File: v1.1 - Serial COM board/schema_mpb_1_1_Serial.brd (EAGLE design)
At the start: 93.3 x 48.5 mm, 76 parts, among them U4 MAX232PTH, U5 MAX232PTH, U6 MAX232PTH

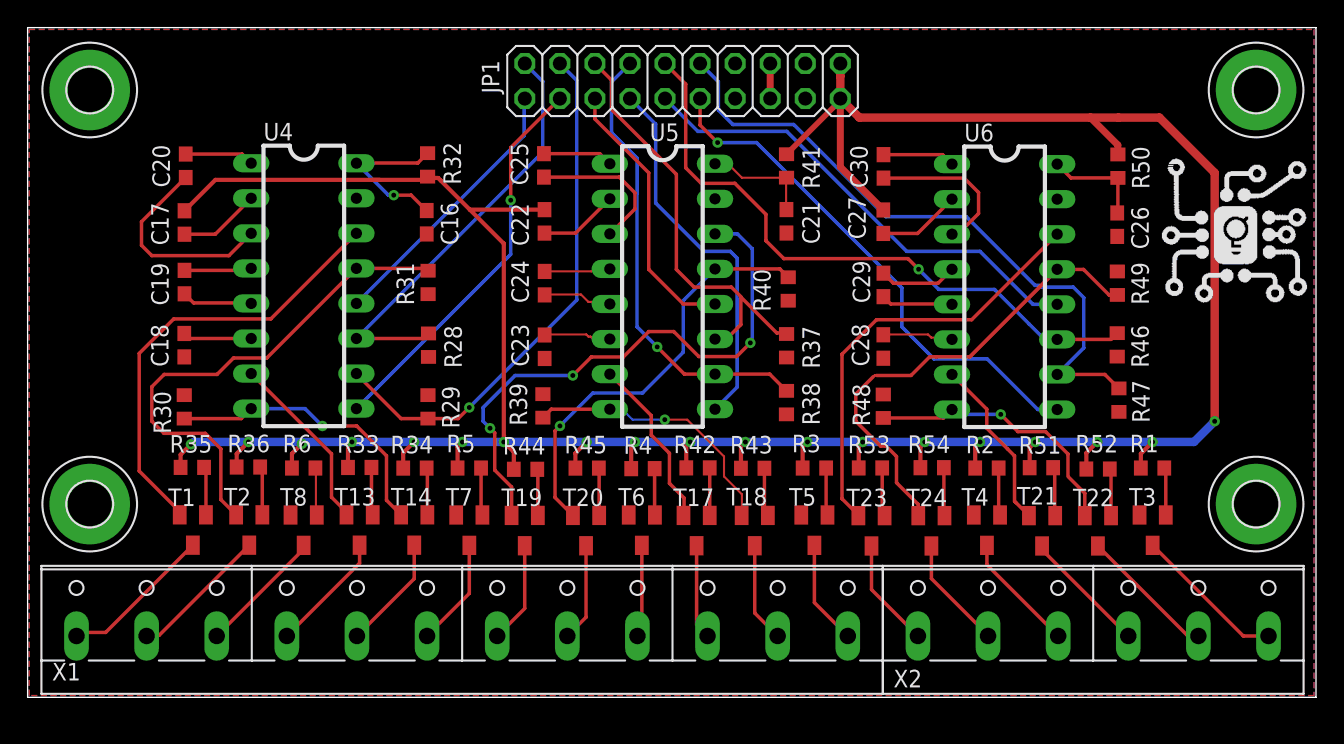
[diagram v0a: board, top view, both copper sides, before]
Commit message: IO and Serial
- Rounded corners
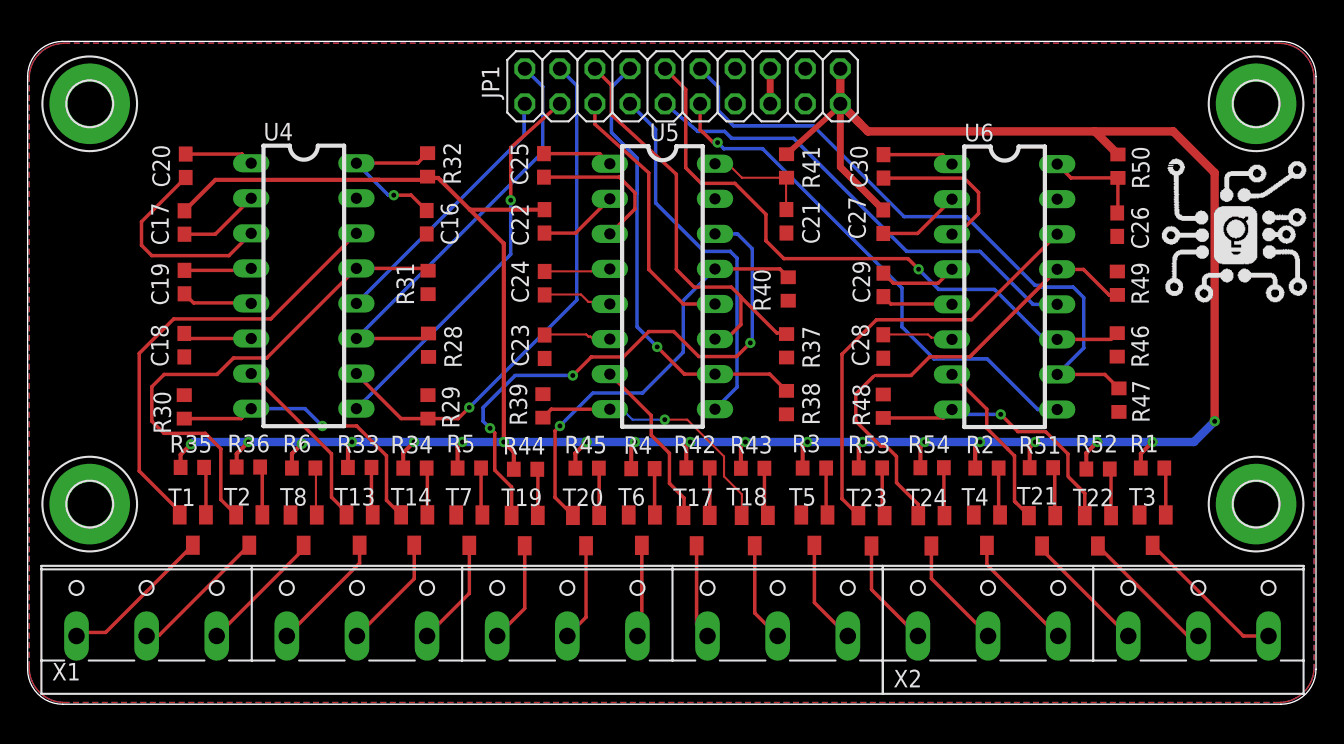
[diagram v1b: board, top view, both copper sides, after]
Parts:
- moved H3 1.00 mm to (3.50, 43.0)
- moved H4 1.00 mm to (88.0, 43.0)
- moved JP1 0.38 mm to (46.5, 44.3)
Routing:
- net +3V3: track 238.2 -> 236.4 mm
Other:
- board size 93.3 x 48.5 mm -> 93.3 x 48 mm

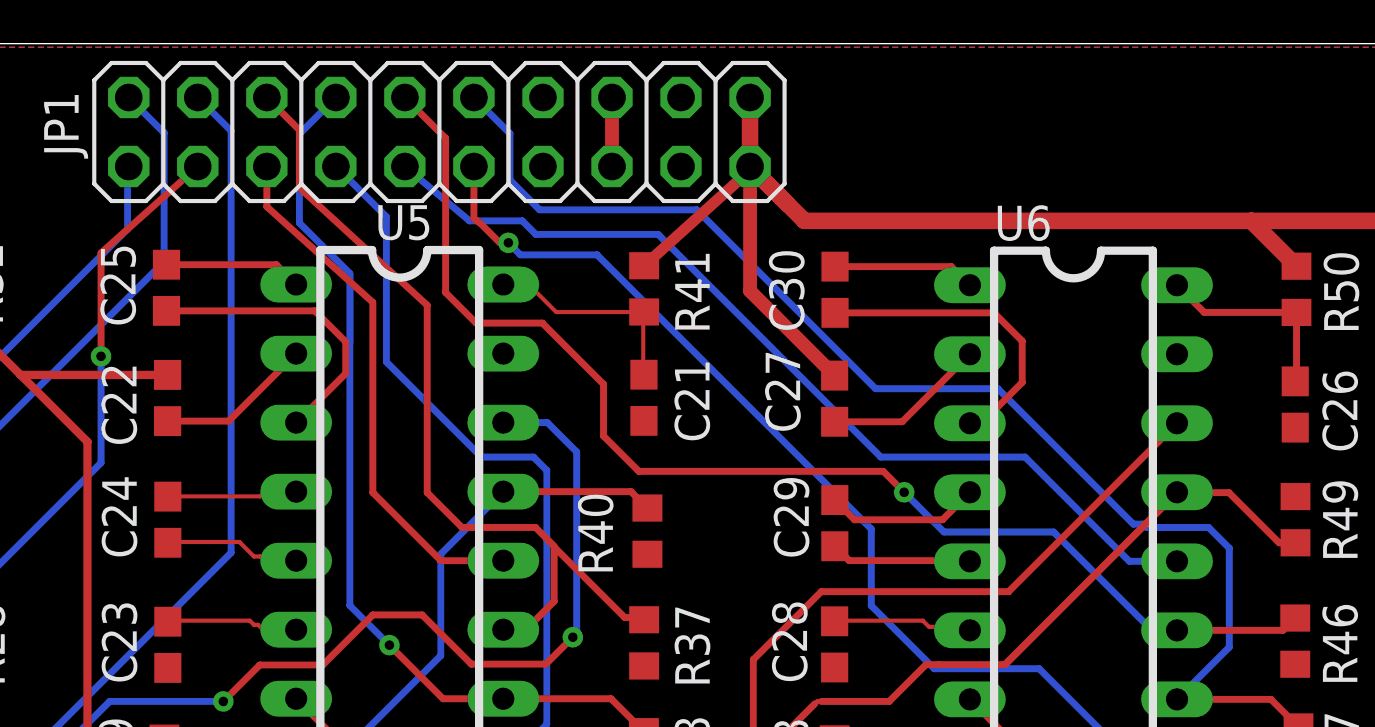
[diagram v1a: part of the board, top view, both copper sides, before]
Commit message: IO board revision
- Made Output traces thicker
- Added pad for 5V/3.3V power for input sensors
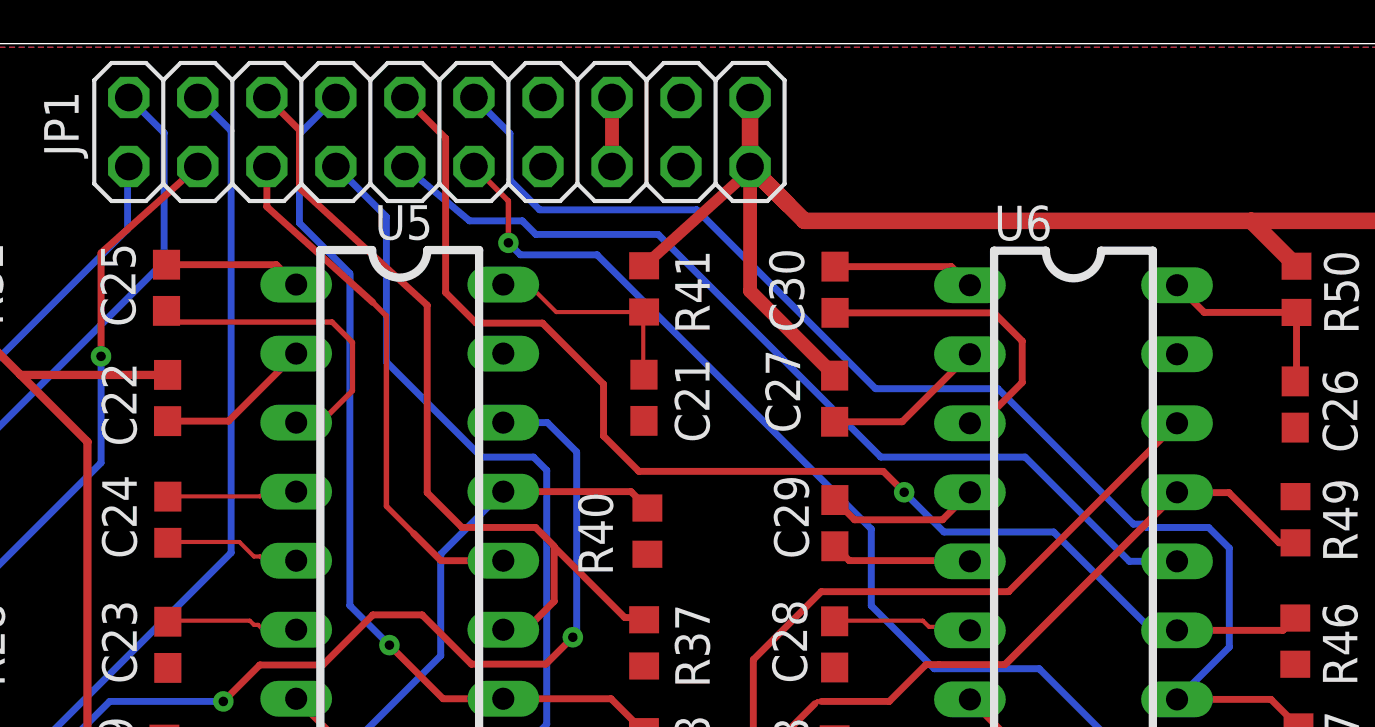
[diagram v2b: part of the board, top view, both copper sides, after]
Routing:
- net N$45: track 11.0 -> 11.8 mm
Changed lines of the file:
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@@
 <wire x1="41.2242" y1="33.6042" x2="41.2242" y2="33.7566" width="0.1524" layer="1"/>
 <wire x1="41.2242" y1="33.6042" x2="41.18" y2="33.576" width="0.1524" layer="1"/>
-<wire x1="36.409" y1="37.687" x2="41.866" y2="37.687" width="0.254" layer="1"/>
-<wire x1="41.866" y1="37.687" x2="43.0022" y2="36.5508" width="0.254" layer="1"/>
-<wire x1="43.0022" y1="35.3822" x2="41.2242" y2="33.6042" width="0.254" layer="1"/>
-<wire x1="43.0022" y1="36.5508" x2="43.0022" y2="35.3822" width="0.254" layer="1"/>
+<wire x1="41.31" y1="33.69" x2="41.2242" y2="33.6042" width="0.254" layer="1"/>
+<wire x1="42.19" y1="33.69" x2="41.31" y2="33.69" width="0.2" layer="1"/>
+<wire x1="43.25" y1="34.75" x2="42.19" y2="33.69" width="0.2" layer="1"/>
+<wire x1="42.5" y1="37.2765" x2="43.25" y2="36.5265" width="0.2" layer="1"/>
+<wire x1="43.25" y1="36.5265" x2="43.25" y2="34.75" width="0.2" layer="1"/>
+<wire x1="36.409" y1="37.687" x2="36.8195" y2="37.2765" width="0.2" layer="1"/>
+<wire x1="36.8195" y1="37.2765" x2="42.5" y2="37.2765" width="0.2" layer="1"/>
 </signal>
 <signal name="N$46">
@@
 <wire x1="40.1" y1="42.999" x2="40.1" y2="41.519" width="0.254" layer="1"/>
 <wire x1="40.1" y1="41.519" x2="44" y2="38" width="0.254" layer="1"/>
-<wire x1="44" y1="38" x2="44" y2="31" width="0.254" layer="1"/>
 <wire x1="46.504" y1="28.496" x2="48.8" y2="28.496" width="0.254" layer="1"/>
-<wire x1="44" y1="31" x2="46.504" y2="28.496" width="0.254" layer="1"/>
+<wire x1="45.5" y1="29.5" x2="46.504" y2="28.496" width="0.254" layer="1"/>
+<wire x1="44" y1="38" x2="44.5" y2="37.5" width="0.2" layer="1"/>
+<wire x1="44.5" y1="30.5" x2="45.5" y2="29.5" width="0.2" layer="1"/>
+<wire x1="44.5" y1="37.5" x2="44.5" y2="30.5" width="0.2" layer="1"/>
 </signal>
 <signal name="RX4">
@@
 <contactref element="U6" pad="9"/>
 <via x="48.9886" y="40.1908" extent="1-16" drill="0.35"/>
-<wire x1="47.72" y1="42.999" x2="47.72" y2="41.0784" width="0.254" layer="1"/>
-<wire x1="47.72" y1="41.0784" x2="47.944803125" y2="40.9211125" width="0.254" layer="1"/>
 <wire x1="62.3397" y1="29.6603" x2="62.3397" y2="26.8397" width="0.254" layer="16"/>
 <wire x1="52.25" y1="39.75" x2="62.3397" y2="29.6603" width="0.254" layer="16"/>
@@
 <wire x1="68.5201" y1="24.5201" x2="72.1882" y2="20.852" width="0.254" layer="16"/>
 <wire x1="72.1882" y1="20.852" x2="73.59" y2="20.852" width="0.254" layer="16"/>
-<wire x1="47.944803125" y1="40.9211125" x2="48.675115625" y2="40.1908" width="0.254" layer="1"/>
-<wire x1="48.675115625" y1="40.1908" x2="48.9886" y2="40.1908" width="0.254" layer="1"/>
 <wire x1="48.9886" y1="40.1908" x2="49.4294" y2="39.75" width="0.254" layer="16"/>
 <wire x1="49.4294" y1="39.75" x2="52.25" y2="39.75" width="0.254" layer="16"/>
+<wire x1="48.9886" y1="40.1908" x2="48.9886" y2="41.7304" width="0.2" layer="1"/>
+<wire x1="48.9886" y1="41.7304" x2="47.72" y2="42.999" width="0.2" layer="1"/>
 </signal>
 <signal name="+5V">
@@
 <wire x1="75.5142" y1="28.956" x2="74.7522" y2="29.718" width="0.254" layer="16"/>
 <wire x1="75.5142" y1="25.3162" x2="75.5142" y2="28.956" width="0.254" layer="16"/>
-<wire x1="74.7522" y1="29.718" x2="72.4662" y2="29.718" width="0.254" layer="16"/>
+<wire x1="74.7522" y1="29.718" x2="74.5" y2="29.718" width="0.254" layer="16"/>
+<wire x1="74.5" y1="29.718" x2="72.4662" y2="29.718" width="0.254" layer="16"/>
 <wire x1="72.4662" y1="29.718" x2="72.3421" y2="29.8421" width="0.254" layer="16"/>
 <wire x1="72.3421" y1="29.8421" x2="71.9813" y2="29.8421" width="0.254" layer="16"/>

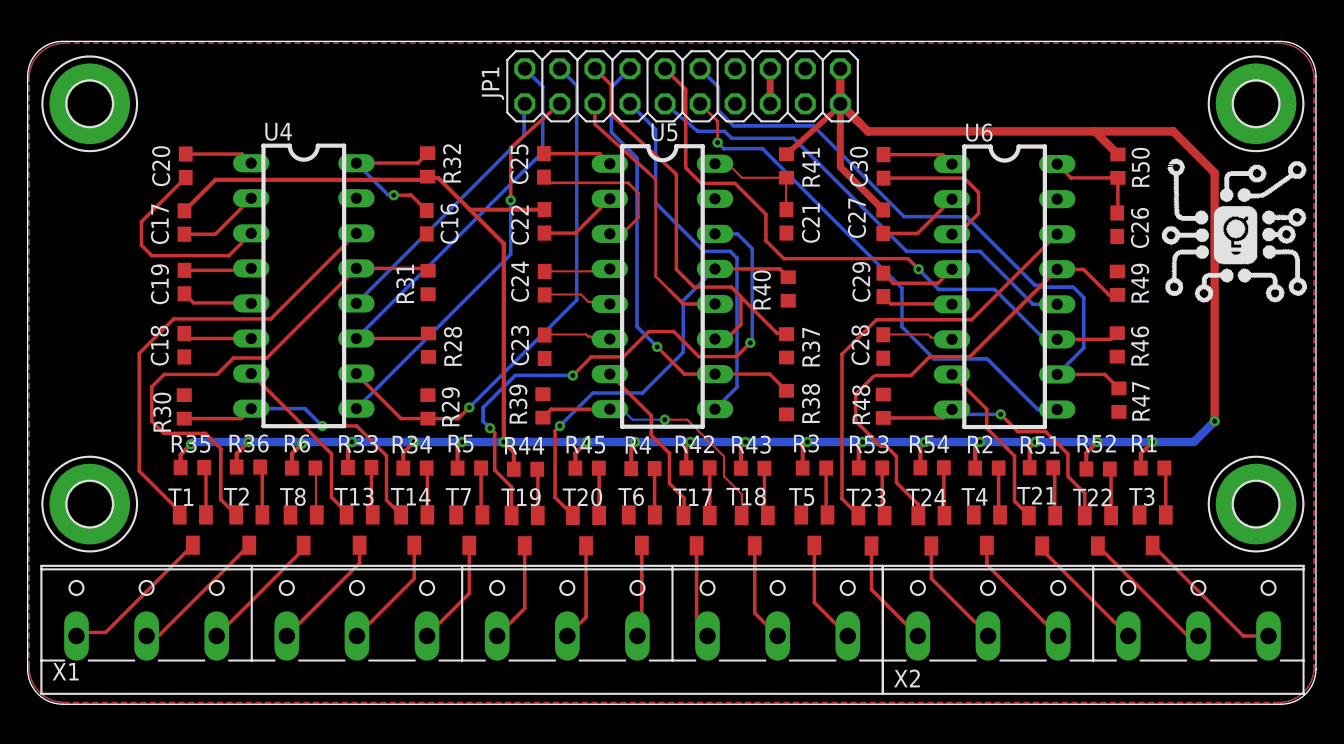
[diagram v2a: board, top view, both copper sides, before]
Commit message: Serial Board Revision
- Labelled terminals
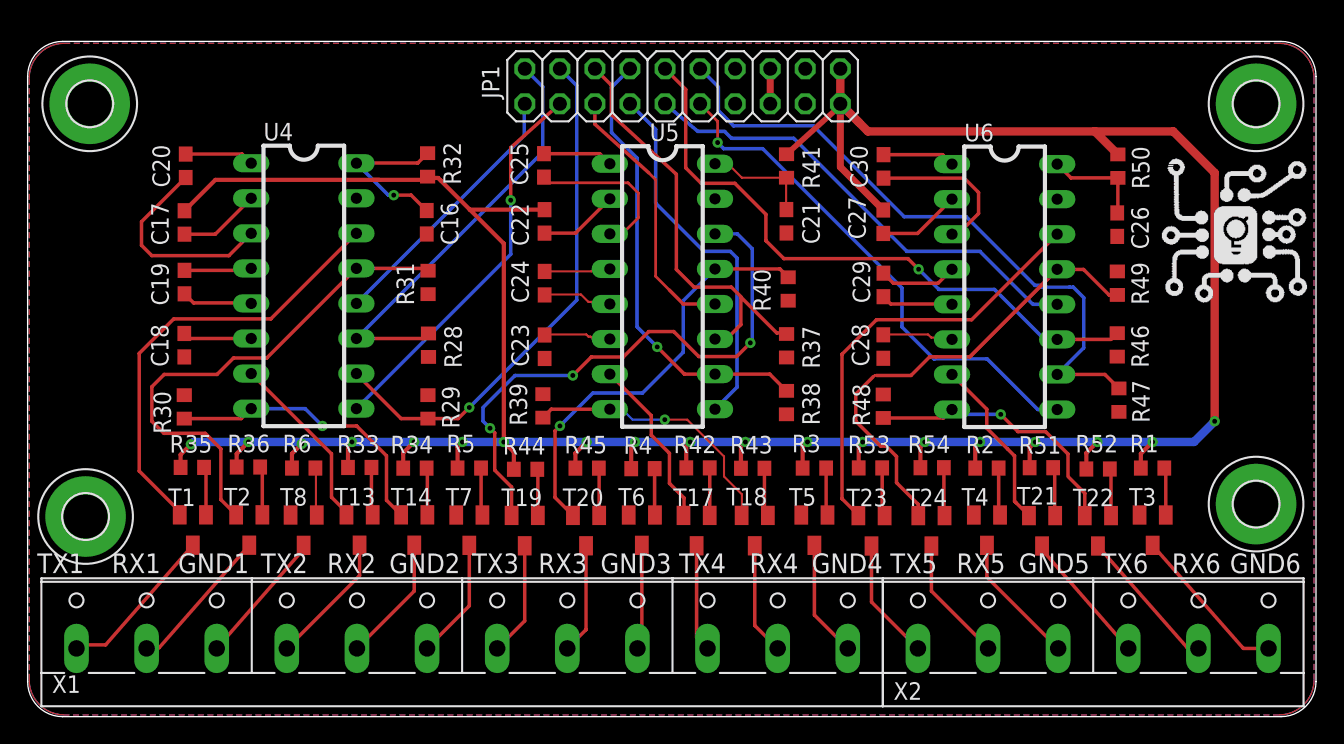
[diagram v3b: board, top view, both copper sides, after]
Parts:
- moved H1 0.95 mm to (3.20, 13.1)
- moved X1 0.90 mm to (30.5, 4.18)
- moved X2 0.90 mm to (76.2, 4.18)
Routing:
- net RXD2#: track 8.29 -> 9.19 mm
- net RXD4#: track 7.22 -> 8.12 mm
- net TXD4#: track 6.86 -> 7.76 mm
- net TXD3#: track 7.36 -> 8.26 mm
- net RXD5#: track 8.22 -> 9.12 mm
- net GND5: track 8.70 -> 9.60 mm
- net GND4: track 7.57 -> 8.47 mm
- net GND2: track 7.83 -> 8.73 mm
- net TXD5#: track 7.91 -> 8.81 mm
- net RXD3#: track 7.10 -> 8.00 mm
- net GND3: track 6.70 -> 7.60 mm
- net TXD2#: track 8.76 -> 9.66 mm
- net TXD6#: track 9.11 -> 9.76 mm
- net GND1: track 9.18 -> 9.83 mm
- net TXD1#: track 11.2 -> 11.8 mm
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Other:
- board size 93.3 x 48 mm -> 93.3 x 48.9 mm
- board text added: "GND1"
- board text added: "GND2"
- board text added: "GND3"
- board text added: "GND4"
- board text added: "GND5"
- board text added: "GND6"
- board text added: "RX1"
- board text added: "RX2"
- board text added: "RX3"
- board text added: "RX4"
- board text added: "RX5"
- board text added: "RX6"
- board text added: "TX1"
- board text added: "TX2"
- board text added: "TX3"
- board text added: "TX4"
- board text added: "TX5"
- board text added: "TX6"
